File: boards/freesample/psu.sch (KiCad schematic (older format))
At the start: 117 parts, among them U26 MCP1755ST-5002E/MC, U27 LM27761, U28 ADP1763Z-1.0, U29 ADP1763Z-1.0, U30 OKL-T/3-W12P-C, U31 ADP1741, U32 OKL-T/3-W12P-C, U33 ADP1741, U34 ADP1741, U35 OKL-T/3-W12P-C, U36 OKL-T/3-W12P-C, U37 LM27761, U38 OKL-T/3-W12P-C, U39 LM27761, U42 ADP1741, U43 ADP1741

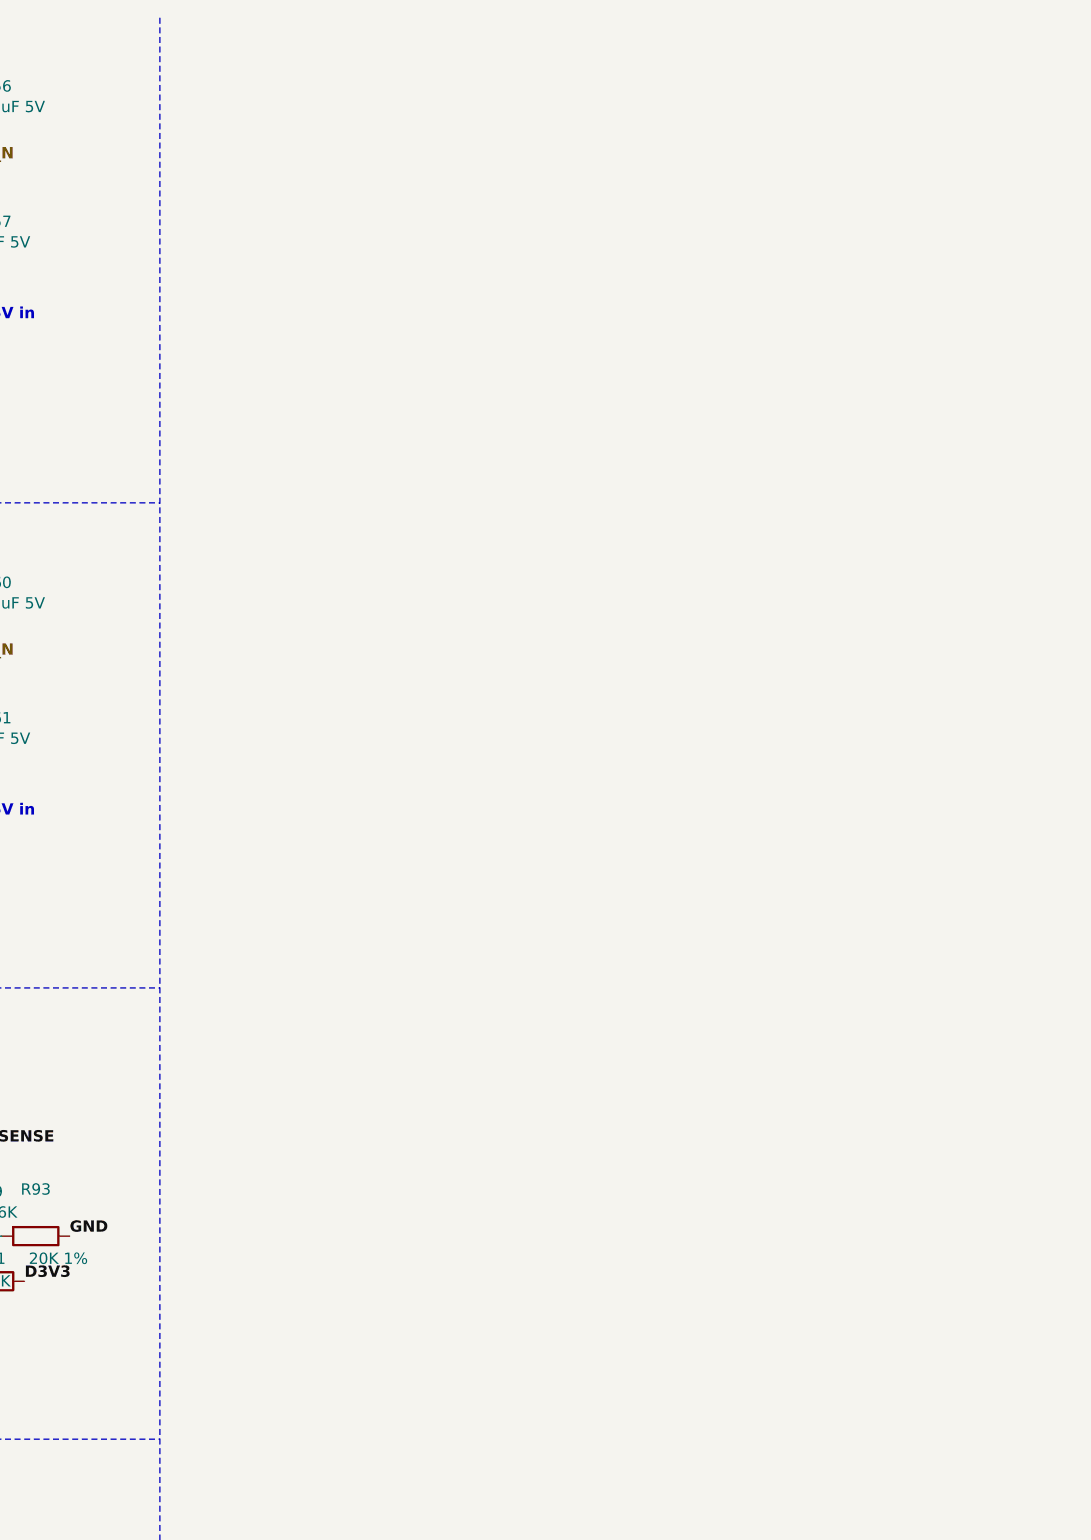
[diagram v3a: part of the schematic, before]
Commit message: Continued design review. Added test points on all power rails.
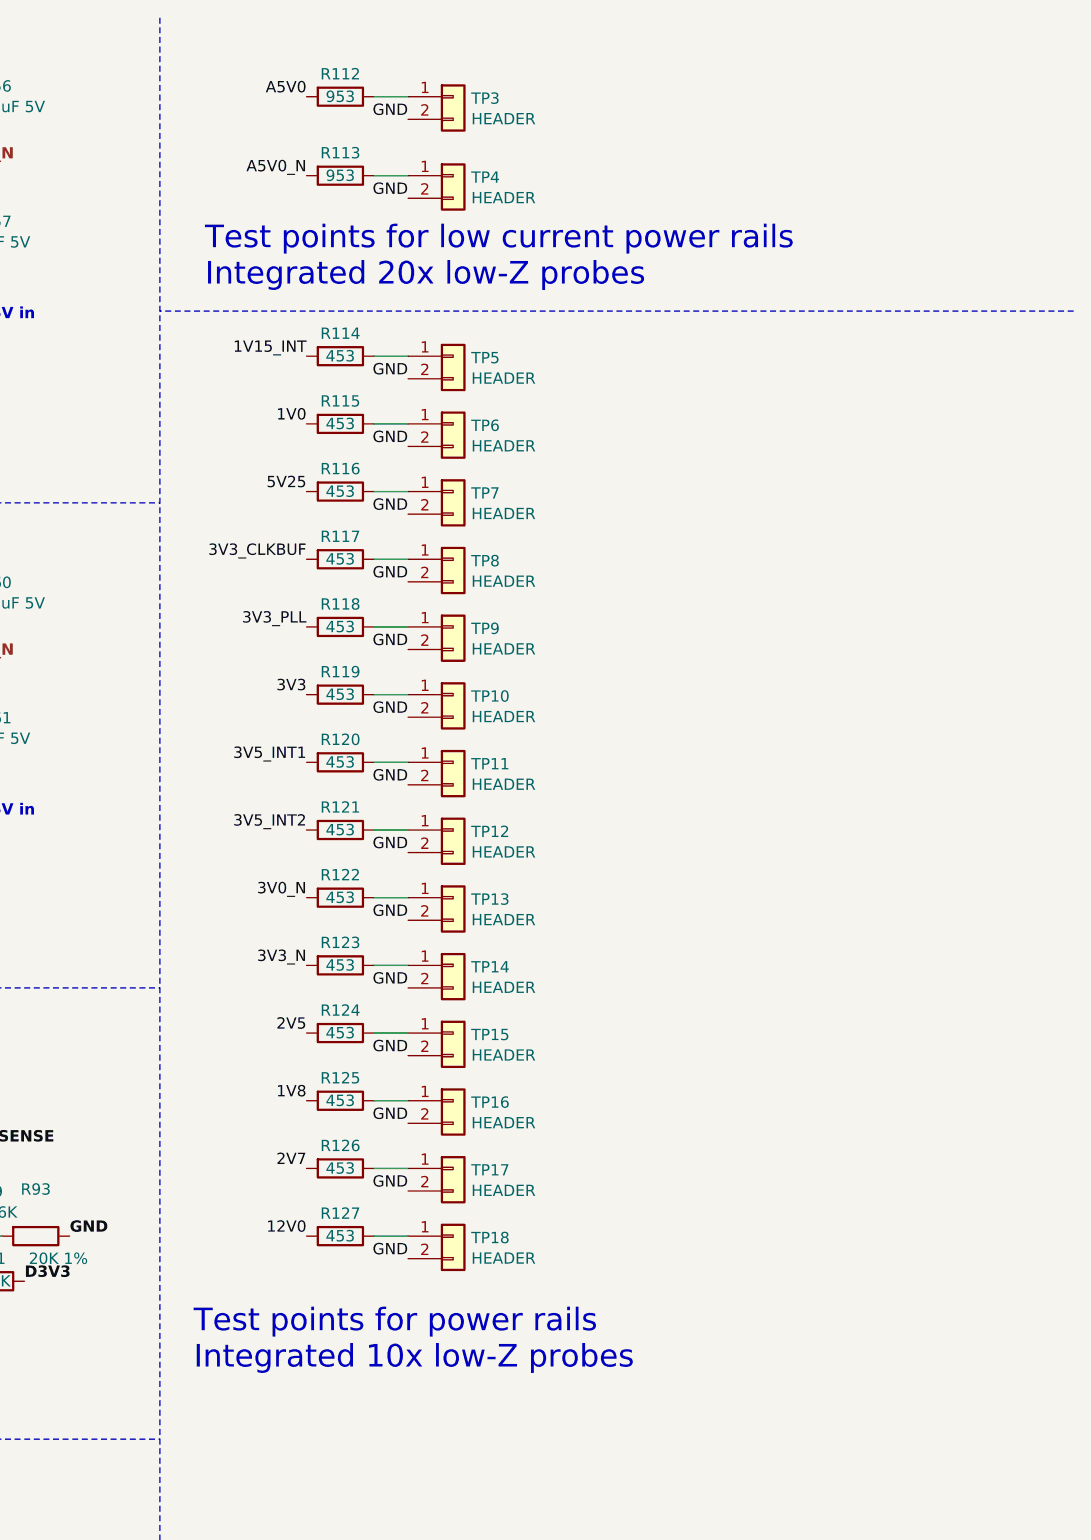
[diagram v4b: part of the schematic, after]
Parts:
- added R112, R113: 953, azonenberg_pcb:EIA_0402_RES_NOSILK, symbol device:R
- added R114, R115, R116, R117, R118, R119, R120, R121, R122, R123, R124, R125, R126, R127: 453, azonenberg_pcb:EIA_0402_RES_NOSILK, symbol device:R
- added TP10, TP11, TP12, TP13, TP14, TP15, TP16, TP17, TP18, TP3, TP4, TP5, TP6, TP7, TP8, TP9: HEADER, azonenberg_pcb:CONN_HEADER_2.54MM_1x2, symbol Connector:Conn_01x02
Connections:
- net 12V0: now also R127.2
- net 1V0: now also R115.2
- net 1V15_INT: now also R114.2
- net 1V8: now also R125.2
- net 2V5: now also R124.2
- net 3V0_N: now also R122.2
- net 3V3: now also R119.2
- net 3V3_CLKBUF: now also R117.2
- net 3V3_N: now also R123.2
- net 3V3_PLL: now also R118.2
- net 3V5_INT1: now also R120.2
- net 3V5_INT2: now also R121.2
- net 5V25: now also R116.2
- net A5V0: now also R112.2
- net GND: now also TP10.2 (Pin_2), TP11.2 (Pin_2), TP12.2 (Pin_2), TP13.2 (Pin_2), TP14.2 (Pin_2), TP15.2 (Pin_2), TP16.2 (Pin_2), TP17.2 (Pin_2), TP18.2 (Pin_2), TP3.2 (Pin_2), TP4.2 (Pin_2), TP5.2 (Pin_2), TP6.2 (Pin_2), TP7.2 (Pin_2), TP8.2 (Pin_2), TP9.2 (Pin_2)
- new net: R112.1, TP3.1 (Pin_1)
- new net: R113.1, TP4.1 (Pin_1)
- new net: R114.1, TP5.1 (Pin_1)
- new net: R115.1, TP6.1 (Pin_1)
- new net: R116.1, TP7.1 (Pin_1)
- new net: R117.1, TP8.1 (Pin_1)
- new net: R118.1, TP9.1 (Pin_1)
- new net: R119.1, TP10.1 (Pin_1)
- new net: R120.1, TP11.1 (Pin_1)
- new net: R121.1, TP12.1 (Pin_1)
- new net: R122.1, TP13.1 (Pin_1)
- new net: R123.1, TP14.1 (Pin_1)
- new net: R124.1, TP15.1 (Pin_1)
- new net: R125.1, TP16.1 (Pin_1)
- new net: R126.1, TP17.1 (Pin_1)
- new net: R127.1, TP18.1 (Pin_1)
- new net 2V7: R126.2
- new net A5V0_N: R113.2
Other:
- note added: "Test points for low current power rails\nIntegrated 20x low-Z probes"
- note added: "Test points for power rails\nIntegrated 10x low-Z probes"

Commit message: Continued schematic review. Significantly simplified one-shot to reduce jitter, board area, and power consumption
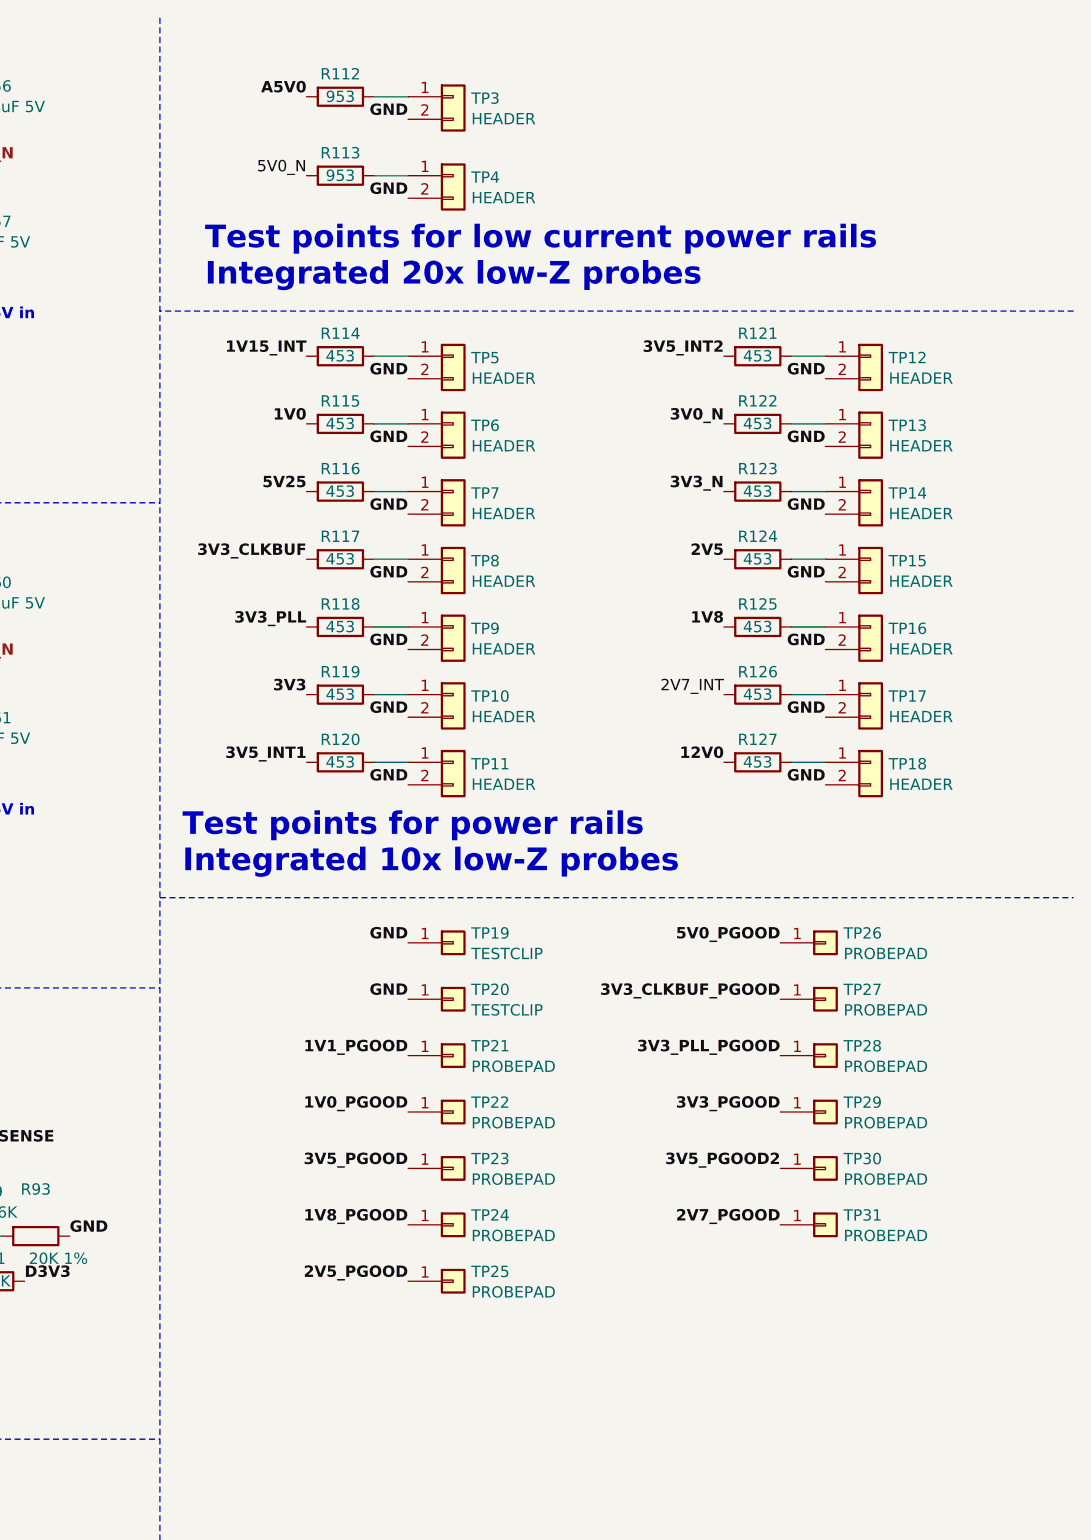
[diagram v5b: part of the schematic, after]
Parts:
- added TP19, TP20: TESTCLIP, azonenberg_pcb:TESTPOINT_SMT_KEYSTONE_5016, symbol Connector:Conn_01x01
- added TP21, TP22, TP23, TP24, TP25, TP26, TP27, TP28, TP29, TP30, TP31: PROBEPAD, azonenberg_pcb:TESTPOINT_SMT_0.5MM, symbol Connector:Conn_01x01
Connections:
- net 2V7 is gone; now on net 2V7_INT: R126.2
- net A5V0_N is gone; now on net 5V0_N: R113.2
- net 1V0_PGOOD: now also TP22.1 (Pin_1)
- net 1V1_PGOOD: now also TP21.1 (Pin_1)
- net 1V8_PGOOD: now also TP24.1 (Pin_1)
- net 2V5_PGOOD: now also TP25.1 (Pin_1)
- net 2V7_PGOOD: now also TP31.1 (Pin_1)
- net 3V3_CLKBUF_PGOOD: now also TP27.1 (Pin_1)
- net 3V3_PGOOD: now also TP29.1 (Pin_1)
- net 3V3_PLL_PGOOD: now also TP28.1 (Pin_1)
- net 3V5_PGOOD: now also TP23.1 (Pin_1)
- net 3V5_PGOOD2: now also TP30.1 (Pin_1)
- net 5V0_PGOOD: now also TP26.1 (Pin_1)
- net GND: now also TP19.1 (Pin_1), TP20.1 (Pin_1)
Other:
- moved on the sheet: R121, R122, R123, R124, R125, R126, R127, TP12, TP13, TP14, TP15, TP16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

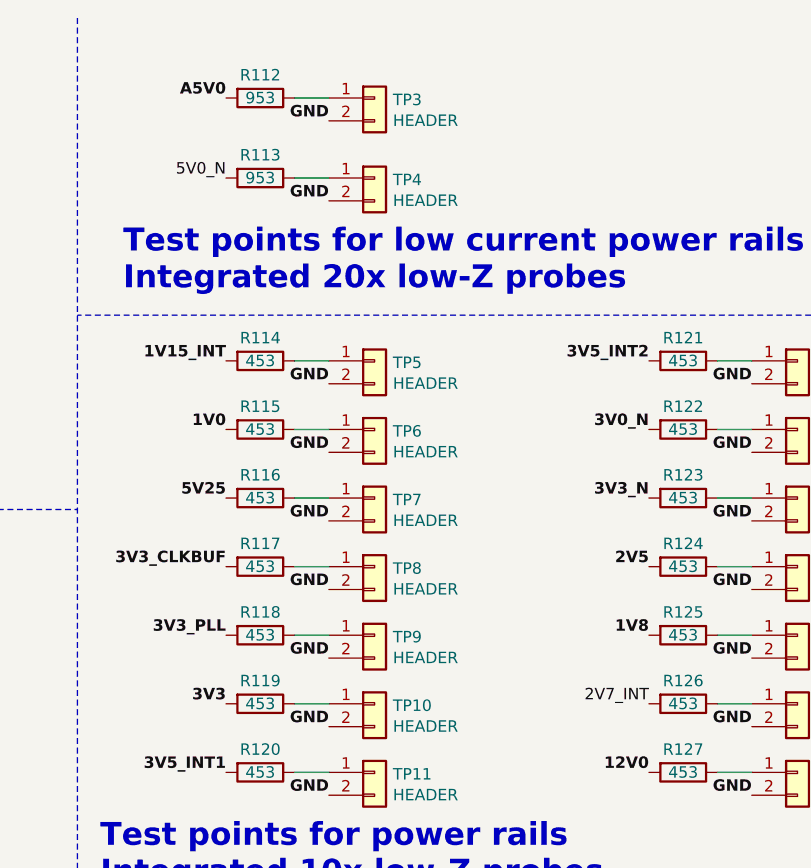
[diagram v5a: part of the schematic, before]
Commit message: Continued design review. Changed termination on DFFs to 1V8. Added some pull resistors to keep DFFs in reset during boot.
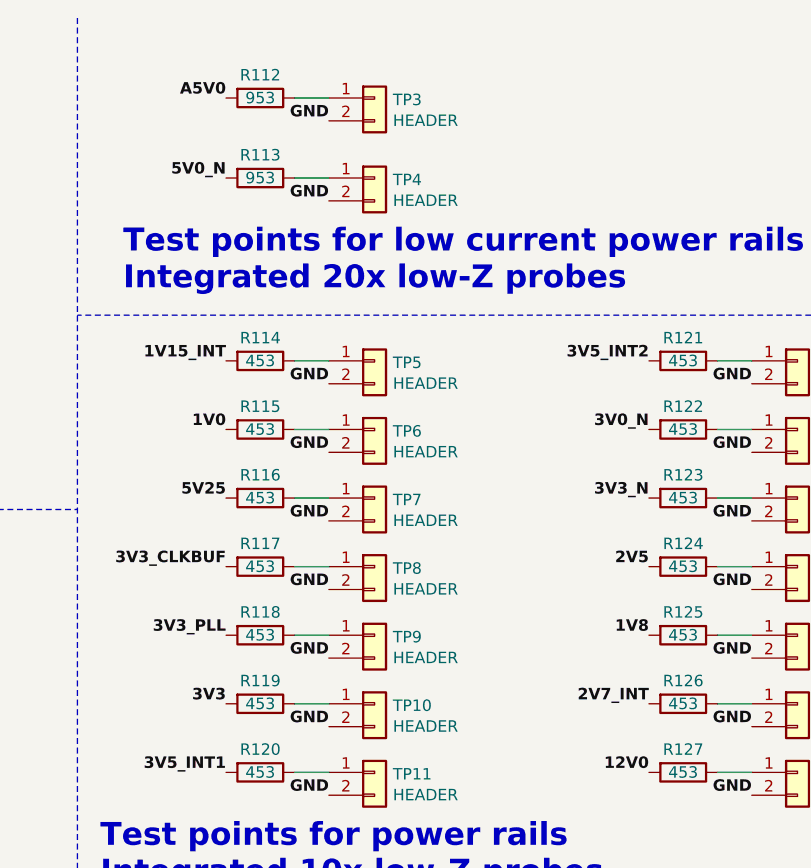
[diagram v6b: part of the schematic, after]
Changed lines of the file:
@@
 Sheet 10 12
 Title "FREESAMPLE Oscilloscope"
-Date "2019-03-16"
+Date "2019-03-17"
 Rev "0.1"
 Comp "Andrew D. Zonenberg / Antikernel Labs"
@@
 Wire Wire Line
 	12950 1200 13100 1200
-Text Label 12650 1200 2    50   ~ 0
+Text Label 12650 1200 2    50   ~ 6
 5V0_N
 Text Notes 12200 1700 0    100  ~ 6
@@
 Wire Wire Line
 	14800 3500 14950 3500
-Text Label 14500 3500 2    50   ~ 0
+Text Label 14500 3500 2    50   ~ 6
 2V7_INT
 $Comp

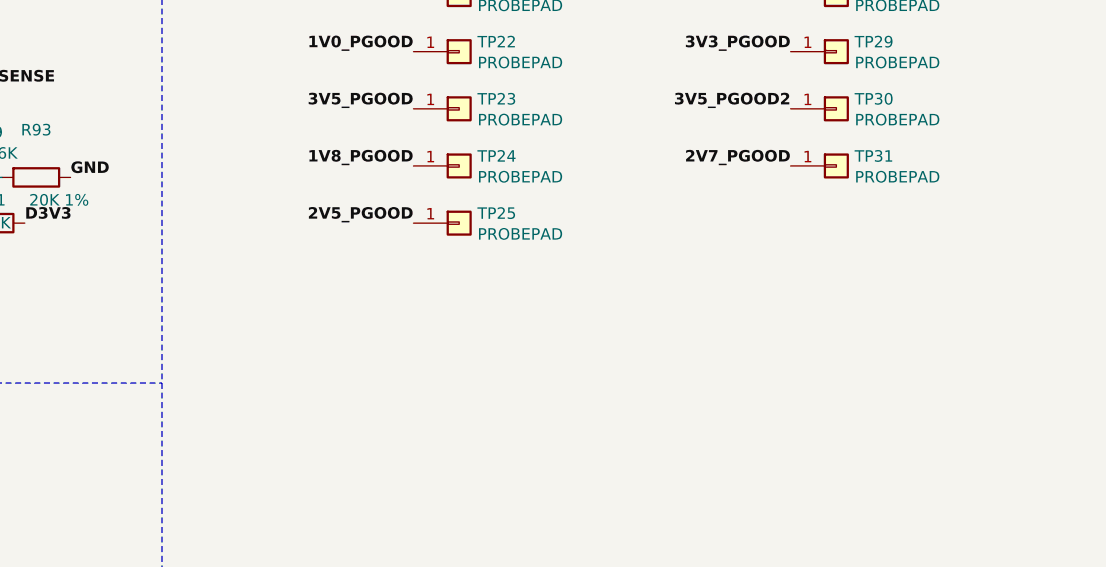
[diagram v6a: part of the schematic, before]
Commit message: Continued work on schematic review. Added some more pull resistors.
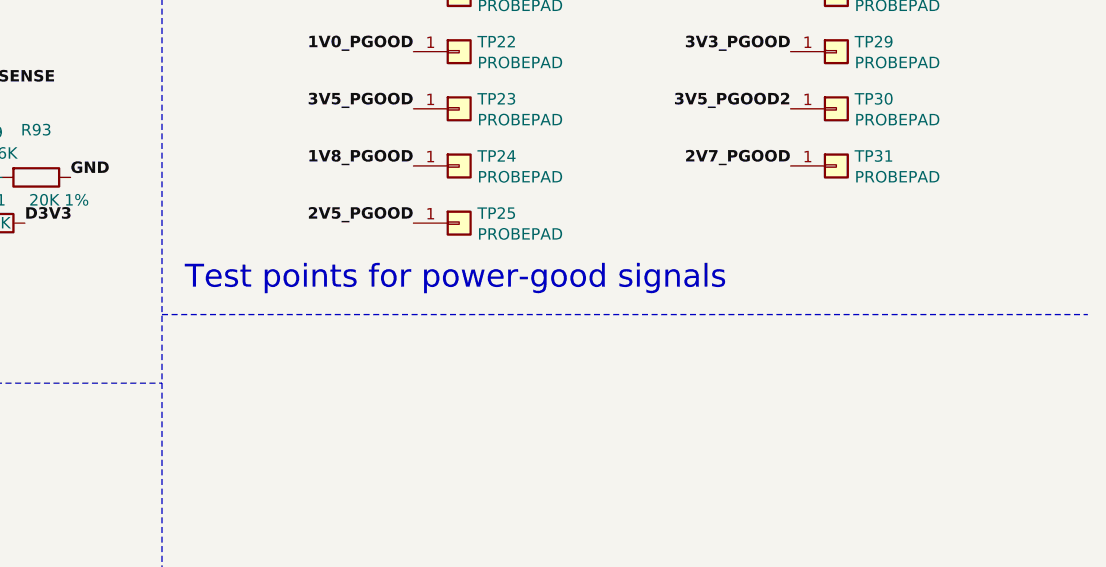
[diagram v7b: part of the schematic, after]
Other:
- note added: "Test points for power-good signals"
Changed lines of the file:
@@
 	1    0    0    -1
 $EndComp
+Text Notes 12100 6400 0    100  ~ 0
+Test points for power-good signals
+Wire Notes Line width 20 style solid
+	12000 6500 16050 6500
 $EndSCHEMATC
